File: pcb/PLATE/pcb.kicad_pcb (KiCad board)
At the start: 2 copper layers, 171 x 142 mm, 75 parts, among them SW1 SW_Push, SW10 SW_Push, SW11 SW_Push, SW12 SW_Push, SW13 SW_Push, SW14 SW_Push, SW15 SW_Push, SW16 SW_Push, SW17 SW_Push, SW18 SW_Push, SW19 SW_Push, SW2 SW_Push, SW20 SW_Push, SW21 SW_Push, SW22 SW_Push, SW23 SW_Push, SW24 SW_Push, SW25 SW_Push, SW26 SW_Push, SW27 SW_Push, SW28 SW_Push, SW29 SW_Push, SW3 SW_Push, SW30 SW_Push, SW31 SW_Push, SW32 SW_Push, SW33 SW_Push, SW34 SW_Push, SW4 SW_Push, SW5 SW_Push, SW6 SW_Push, SW7 SW_Push, SW8 SW_Push, SW9 SW_Push

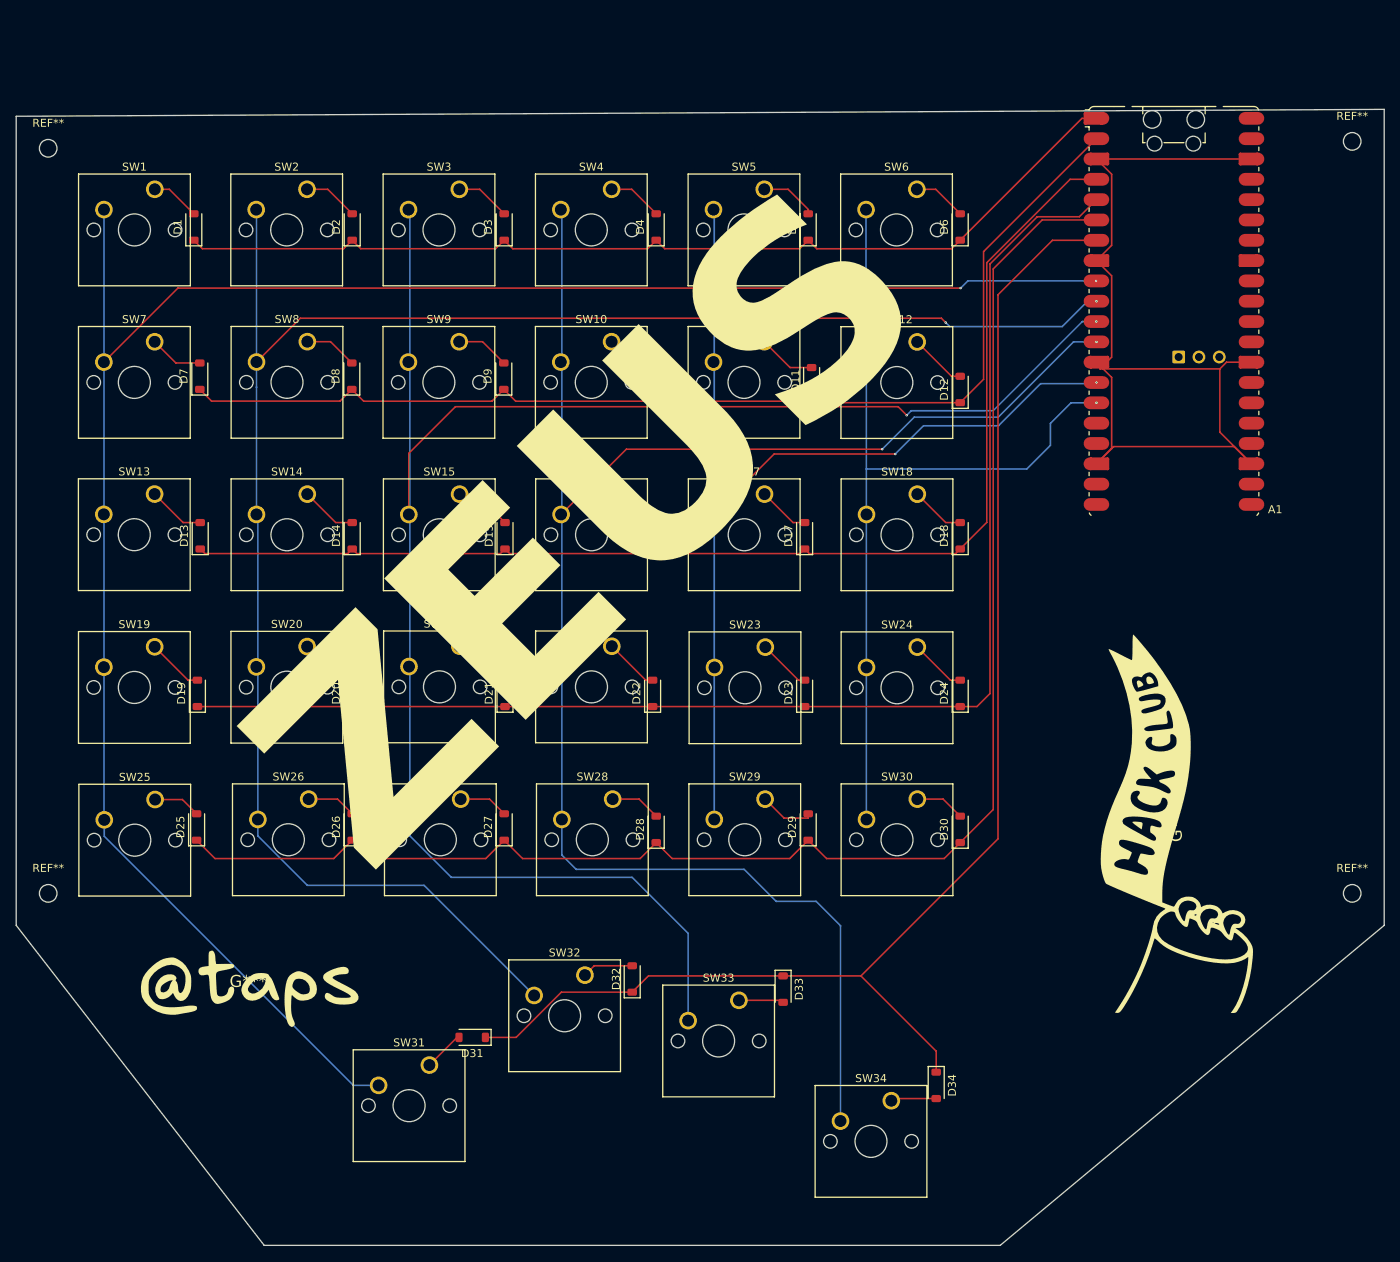
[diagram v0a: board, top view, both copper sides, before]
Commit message: Updated Images with cart
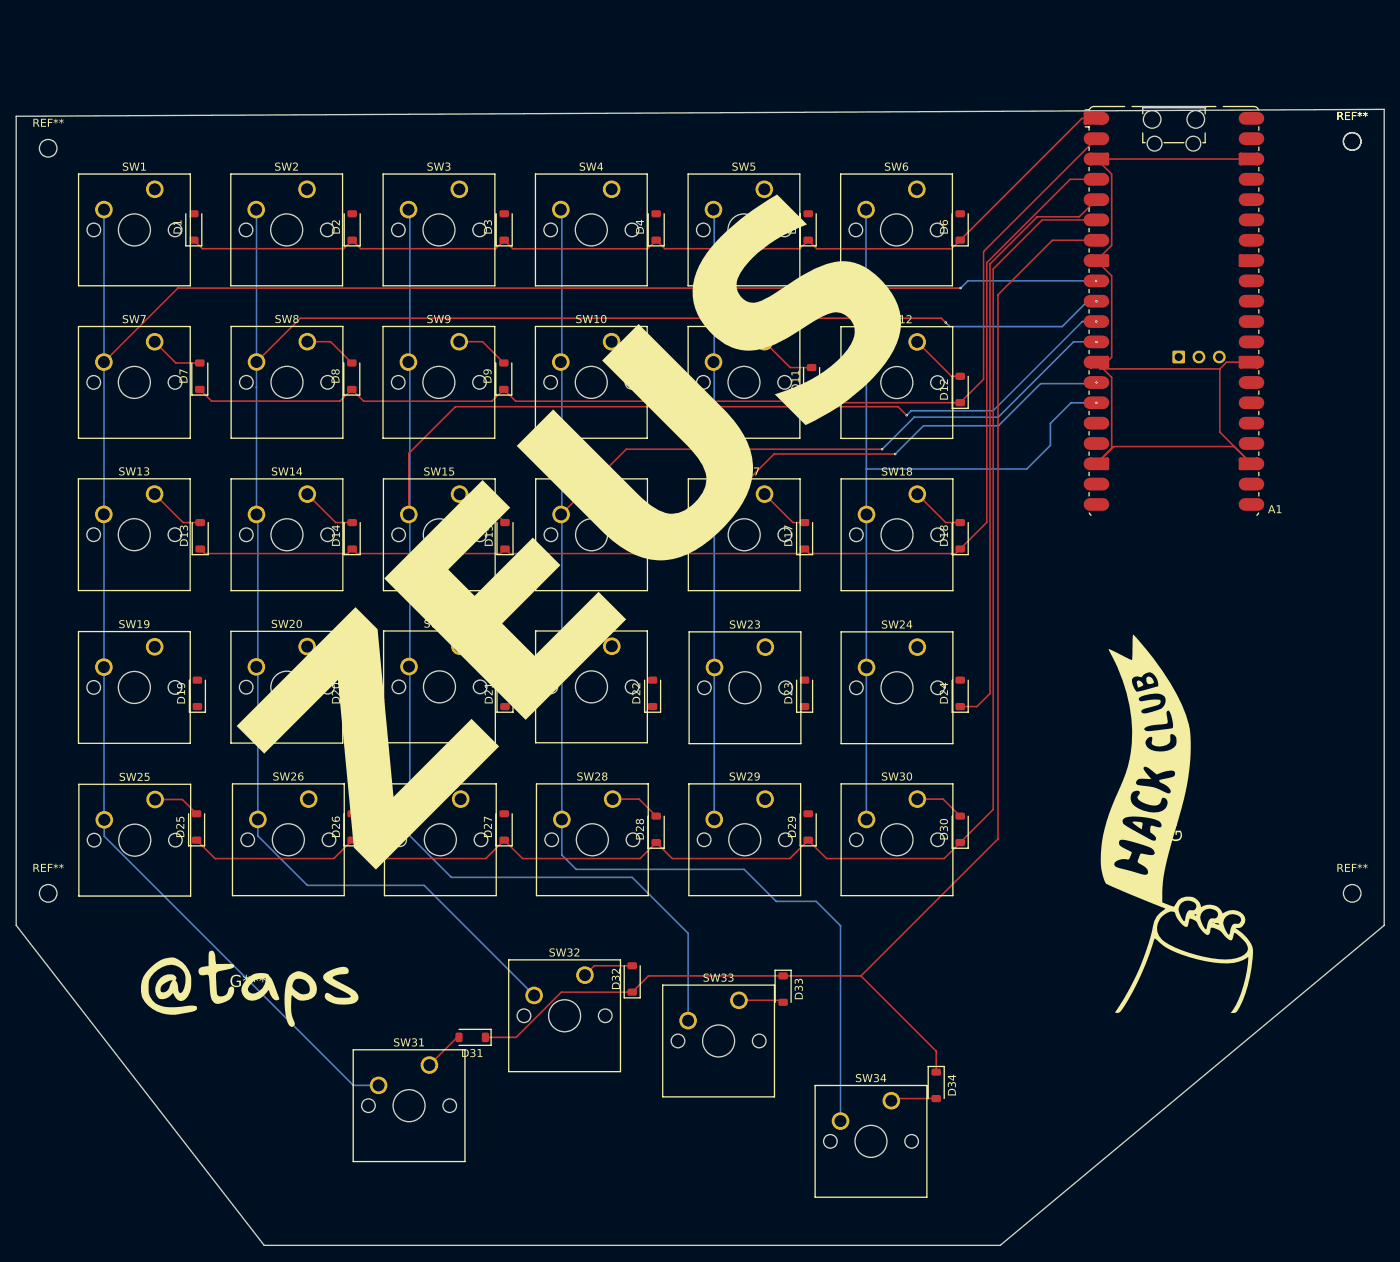
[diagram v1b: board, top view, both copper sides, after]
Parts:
- added REF**: MountingHole_2.2mm_M2, MountingHole:MountingHole_2.2mm_M2, F.Cu at (216.0, 22.0)
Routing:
- net row4: track 170.1 -> 74.7 mm
- net Net-(D21-A): track 7.41 -> 0.00 mm
- net Net-(D20-A): track 7.37 -> 0.00 mm
- net Net-(D5-A): track 7.10 -> 0.00 mm
- net Net-(D24-A): track 7.07 -> 0.00 mm
- net Net-(D19-A): track 7.07 -> 0.00 mm
- net Net-(D2-A): track 6.92 -> 0.00 mm
- net Net-(D29-A): track 6.89 -> 0.00 mm
- net Net-(D3-A): track 6.88 -> 0.00 mm
- net Net-(D22-A): track 6.86 -> 0.00 mm
- net Net-(D4-A): track 6.84 -> 0.00 mm
- net Net-(D6-A): track 6.69 -> 0.00 mm
- net Net-(D23-A): track 6.62 -> 0.00 mm
- net Net-(D27-A): track 6.20 -> 0.00 mm
- net Net-(D26-A): track 6.20 -> 0.00 mm
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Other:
- board size 171 x 142 mm -> 171 x 142.3 mm
